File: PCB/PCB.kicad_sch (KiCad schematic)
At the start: 0 parts

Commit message: add symbols
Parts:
- added J1, J3, J5, J6: Conn_01x06_Socket, Connector_PinHeader_2.54mm:PinHeader_1x06_P2.54mm_Vertical, symbol Connector:Conn_01x06_Socket
- added J2, J4, J7, J8: Conn_01x04_Socket, Connector_PinHeader_2.54mm:PinHeader_1x04_P2.54mm_Vertical, symbol Connector:Conn_01x04_Socket
- added SW1, SW2, SW3: SW_Push, Connector_PinHeader_2.54mm:PinHeader_2x01_P2.54mm_Vertical, symbol Switch:SW_Push
- added U1, U2, U3, U4: HX711, symbol _HX711:HX711_Dev
- added U5: SD1306, Connector_PinHeader_2.54mm:PinHeader_1x04_P2.54mm_Vertical, symbol Display_Graphic:ER_OLEDM0.91_1x-I2C
- added U6: SD1309, Connector_PinHeader_2.54mm:PinHeader_1x04_P2.54mm_Vertical, symbol Display_Graphic:ER_OLEDM0.91_1x-I2C
- added U8: ESP32-DevKitC, PCM_Espressif:ESP32-DevKitC, symbol PCM_Espressif:ESP32-DevKitC
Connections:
- new net: J3.6 (Pin_6), U2.1 (E+)
- new net: J3.5 (Pin_5), U2.2 (E-)
- new net: J3.4 (Pin_4), U2.3 (A-)
- new net: J3.3 (Pin_3), U2.4 (A+)
- new net: J3.2 (Pin_2), U2.5 (B-)
- new net: J3.1 (Pin_1), U2.6 (B+)
- new net: J4.3 (Pin_3), U2.8 (DATA)
- new net: J4.2 (Pin_2), U2.9 (CLK)
- new net: J8.2 (Pin_2), U4.9 (CLK)
- new net: J8.3 (Pin_3), U4.8 (DATA)
- new net: J7.2 (Pin_2), U3.9 (CLK)
- new net: J7.3 (Pin_3), U3.8 (DATA)
- new net: J6.1 (Pin_1), U4.6 (B+)
- new net: J6.2 (Pin_2), U4.5 (B-)
- new net: J6.3 (Pin_3), U4.4 (A+)
- new net: J6.4 (Pin_4), U4.3 (A-)
- new net: J6.5 (Pin_5), U4.2 (E-)
- new net: J6.6 (Pin_6), U4.1 (E+)
- new net: J1.1 (Pin_1), U1.6 (B+)
- new net: J1.2 (Pin_2), U1.5 (B-)
- new net: J1.3 (Pin_3), U1.4 (A+)
- new net: J1.4 (Pin_4), U1.3 (A-)
- new net: J1.5 (Pin_5), U1.2 (E-)
- new net: J1.6 (Pin_6), U1.1 (E+)
- new net: J5.1 (Pin_1), U3.6 (B+)
- new net: J5.2 (Pin_2), U3.5 (B-)
- new net: J5.3 (Pin_3), U3.4 (A+)
- new net: J5.4 (Pin_4), U3.3 (A-)
- new net: J5.5 (Pin_5), U3.2 (E-)
- new net: J5.6 (Pin_6), U3.1 (E+)
- new net: J2.3 (Pin_3), U1.8 (DATA)
- new net: J2.2 (Pin_2), U1.9 (CLK)
- new net +3.3V: J2.1 (Pin_1), J4.1 (Pin_1), J7.1 (Pin_1), J8.1 (Pin_1), SW1.1, SW2.1, SW3.1, U1.10 (VCC), U2.10 (VCC), U3.10 (VCC), U4.10 (VCC), U5.2 (VCC), U6.2 (VCC), U8.1 (3V3)
- new net GND: J2.4 (Pin_4), J4.4 (Pin_4), J7.4 (Pin_4), J8.4 (Pin_4), U1.7 (GND), U2.7 (GND), U3.7 (GND), U4.7 (GND), U5.1 (GND), U6.1 (GND), U8.14 (GND), U8.32 (GND), U8.38 (GND)
- no-connect marks 0 -> 1

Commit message: Connect parts
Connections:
- net BTN1: now reaches SW1.2
- net BTN1: now also U8.27 (GPIO16)
- net DATA2: now reaches J4.3 (Pin_3), U2.8 (DATA)
- net DATA2: now also U8.7 (32K_XP/GPIO32/ADC1_CH4)
- net CLK2: now reaches J4.2 (Pin_2), U2.9 (CLK)
- net CLK2: now also U8.8 (32K_XN/GPIO33/ADC1_CH5)
- net CLK4: now reaches J8.2 (Pin_2), U4.9 (CLK)
- net CLK4: now also U8.12 (MTMS/GPIO14/ADC2_CH6)
- net DATA4: now reaches J8.3 (Pin_3), U4.8 (DATA)
- net DATA4: now also U8.11 (ADC2_CH7/GPIO27)
- net CLK3: now reaches J7.2 (Pin_2), U3.9 (CLK)
- net CLK3: now also U8.10 (DAC_2/ADC2_CH9/GPIO26)
- net DATA3: now reaches J7.3 (Pin_3), U3.8 (DATA)
- net DATA3: now also U8.9 (DAC_1/ADC2_CH8/GPIO25)
- net at U5.3 (SCL): now also U6.3 (SCL), U8.36 (GPIO22)
- net at U5.4 (SDA): now also U6.4 (SDA), U8.33 (GPIO21)
- net BTN3: now reaches SW3.2
- net BTN3: now also U8.29 (GPIO5)
- net BTN2: now reaches U8.28 (GPIO17)
- net BTN2: now also SW2.2
- net DATA1: now reaches U8.30 (GPIO18)
- net DATA1: now also J2.3 (Pin_3), U1.8 (DATA)
- net CLK1: now reaches U8.31 (GPIO19)
- net CLK1: now also J2.2 (Pin_2), U1.9 (CLK)
- no-connect marks 1 -> 21

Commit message: Finished layout
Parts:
- removed J1, J3, J5, J6: Conn_01x06_Socket, Connector_PinHeader_2.54mm:PinHeader_1x06_P2.54mm_Vertical, symbol Connector:Conn_01x06_Socket
- renumbered J2 to J1, J4 to J2, J7 to J3, J8 to J4, U8 to U5, U5 to U6, U6 to U7
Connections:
- no-connect marks 21 -> 45
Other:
- note added: "Adding capacitors will be helpful"

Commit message: update pcb
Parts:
- U5: footprint PCM_Espressif:ESP32-DevKitC -> _custom-footprint:ESP32-DevKitC
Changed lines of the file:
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@@
 			)
 		)
-		(property "Footprint" "PCM_Espressif:ESP32-DevKitC"
+		(property "Footprint" "_custom-footprint:ESP32-DevKitC"
 			(at 173.99 149.86 0)
 			(hide yes)

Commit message: Add capacitor
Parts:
- added C1: 10nf, Capacitor_THT:C_Radial_D5.0mm_H11.0mm_P2.00mm, symbol Device:C_Small_US
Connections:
- net +3.3V: now also C1.1
- net GND: now also C1.2
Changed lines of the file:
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@@
+	)
+	(symbol
+		(lib_id "power:VCC")
+		(at 109.22 171.45 0)
+		(unit 1)
+		(body_style 1)
+		(exclude_from_sim no)
+		(in_bom yes)
+		(on_board yes)
+		(in_pos_files yes)
+		(dnp no)
+		(fields_autoplaced yes)
+		(property "Reference" "#PWR022"
+			(at 109.22 175.26 0)
+			(hide yes)
+			(show_name no)
+			(do_not_autoplace no)
+			(effects
+				(font
+					(size 1.27 1.27)
+				)
+			)
+		)
+		(property "Value" "VCC"
+			(at 109.22 166.37 0)
+			(show_name no)
+			(do_not_autoplace no)
+			(effects
+				(font
+					(size 1.27 1.27)
+				)
+			)
+		)
+		(property "Footprint" ""
+			(at 109.22 171.45 0)
+			(hide yes)
+			(show_name no)
+			(do_not_autoplace no)
+			(effects
+				(font
+					(size 1.27 1.27)
+				)
+			)
+		)
+		(property "Datasheet" ""
+			(at 109.22 171.45 0)
+			(hide yes)
+			(show_name no)
+			(do_not_autoplace no)
+			(effects
+				(font
+					(size 1.27 1.27)
+				)
+			)
+		)
+		(property "Description" "Power symbol creates a global label with name \"VCC\""
+			(at 109.22 171.45 0)
+			(hide yes)
+			(show_name no)
+			(do_not_autoplace no)
+			(effects
+				(font
+					(size 1.27 1.27)
+				)
+			)
+		)
+		(pin "1"
+		)
+		(instances
+			(project "PCB"
+				(path "/dfd5a8fa-84d7-4b09-a8df-d6a914f2fe00"
+					(reference "#PWR022")
+					(unit 1)
+				)
+			)
+		)
 	)
 	(symbol
@@
 	)
 	(symbol
+		(lib_id "power:GND")
+		(at 109.22 176.53 0)
+		(unit 1)
+		(body_style 1)
+		(exclude_from_sim no)
+		(in_bom yes)
+		(on_board yes)
+		(in_pos_files yes)
+		(dnp no)
+		(fields_autoplaced yes)
+		(property "Reference" "#PWR021"
+			(at 109.22 182.88 0)
+			(hide yes)
+			(show_name no)
+			(do_not_autoplace no)
+			(effects
+				(font
+					(size 1.27 1.27)
+				)
+			)
+		)
+		(property "Value" "GND"
+			(at 109.22 181.61 0)
+			(hide yes)
+			(show_name no)
+			(do_not_autoplace no)
+			(effects
+				(font
+					(size 1.27 1.27)
+				)
+			)
+		)
+		(property "Footprint" ""
+			(at 109.22 176.53 0)
+			(hide yes)
+			(show_name no)
+			(do_not_autoplace no)
+			(effects
+				(font
+					(size 1.27 1.27)
+				)
+			)
+		)
+		(property "Datasheet" ""
+			(at 109.22 176.53 0)
+			(hide yes)
+			(show_name no)
+			(do_not_autoplace no)
+			(effects
+				(font
+					(size 1.27 1.27)
+				)
+			)
+		)
+		(property "Description" "Power symbol creates a global label with name \"GND\" , ground"
+			(at 109.22 176.53 0)
+			(hide yes)
+			(show_name no)
+			(do_not_autoplace no)
+			(effects
+				(font
+					(size 1.27 1.27)
+				)
+			)
+		)
+		(pin "1"
+		)
+		(instances
+			(project "PCB"
+				(path "/dfd5a8fa-84d7-4b09-a8df-d6a914f2fe00"
+					(reference "#PWR021")
+					(unit 1)
+				)
+			)
+		)
+	)
+	(symbol
 		(lib_id "_HX711:HX711_Dev")
 		(at 71.12 34.29 0)
@@
 					(unit 1)
 				)
+			)
+		)
+	)
+	(symbol
+		(lib_id "Device:C_Small_US")
+		(at 109.22 173.99 0)
+		(unit 1)
+		(body_style 1)
+		(exclude_from_sim no)
+		(in_bom yes)
+		(on_board yes)
+		(in_pos_files yes)
+		(dnp no)
+		(fields_autoplaced yes)
+		(property "Reference" "C1"
+			(at 111.76 172.8469 0)
+			(show_name no)
+			(do_not_autoplace no)
+			(effects
+				(font
+					(size 1.27 1.27)
+				)
+				(justify left)
+			)
+		)
+		(property "Value" "10nf"
+			(at 111.76 175.3869 0)
+			(show_name no)
+			(do_not_autoplace no)
+			(effects
+				(font
+					(size 1.27 1.27)
+				)
+				(justify left)
+			)
+		)
+		(property "Footprint" "Capacitor_THT:C_Radial_D5.0mm_H11.0mm_P2.00mm"
+			(at 109.22 173.99 0)
+			(hide yes)
+			(show_name no)
+			(do_not_autoplace no)
+			(effects
+				(font
+					(size 1.27 1.27)
+				)
+			)
+		)
+		(property "Datasheet" ""
+			(at 109.22 173.99 0)
+			(hide yes)
+			(show_name no)
+			(do_not_autoplace no)
+			(effects
+				(font
+					(size 1.27 1.27)
+				)
+			)
+		)
+		(property "Description" "capacitor, small US symbol"
+			(at 109.22 173.99 0)
+			(hide yes)
+			(show_name no)
+			(do_not_autoplace no)
+			(effects
+				(font
+					(size 1.27 1.27)
+				)
+			)
+		)
+		(pin "1"
+		)
+		(pin "2"
+		)
+		(instances
+			(project "PCB"
+				(path "/dfd5a8fa-84d7-4b09-a8df-d6a914f2fe00"
+					(reference "C1")
+					(unit 1)
+				)

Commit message: Change push button connection
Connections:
- net +3.3V: no longer SW1.1, SW2.1, SW3.1
- net GND: now also SW1.1, SW2.1, SW3.1
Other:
- note added: "Place capacitor near push buttons"
- note removed: "Adding capacitors will be helpful"
- moved on the sheet: C1

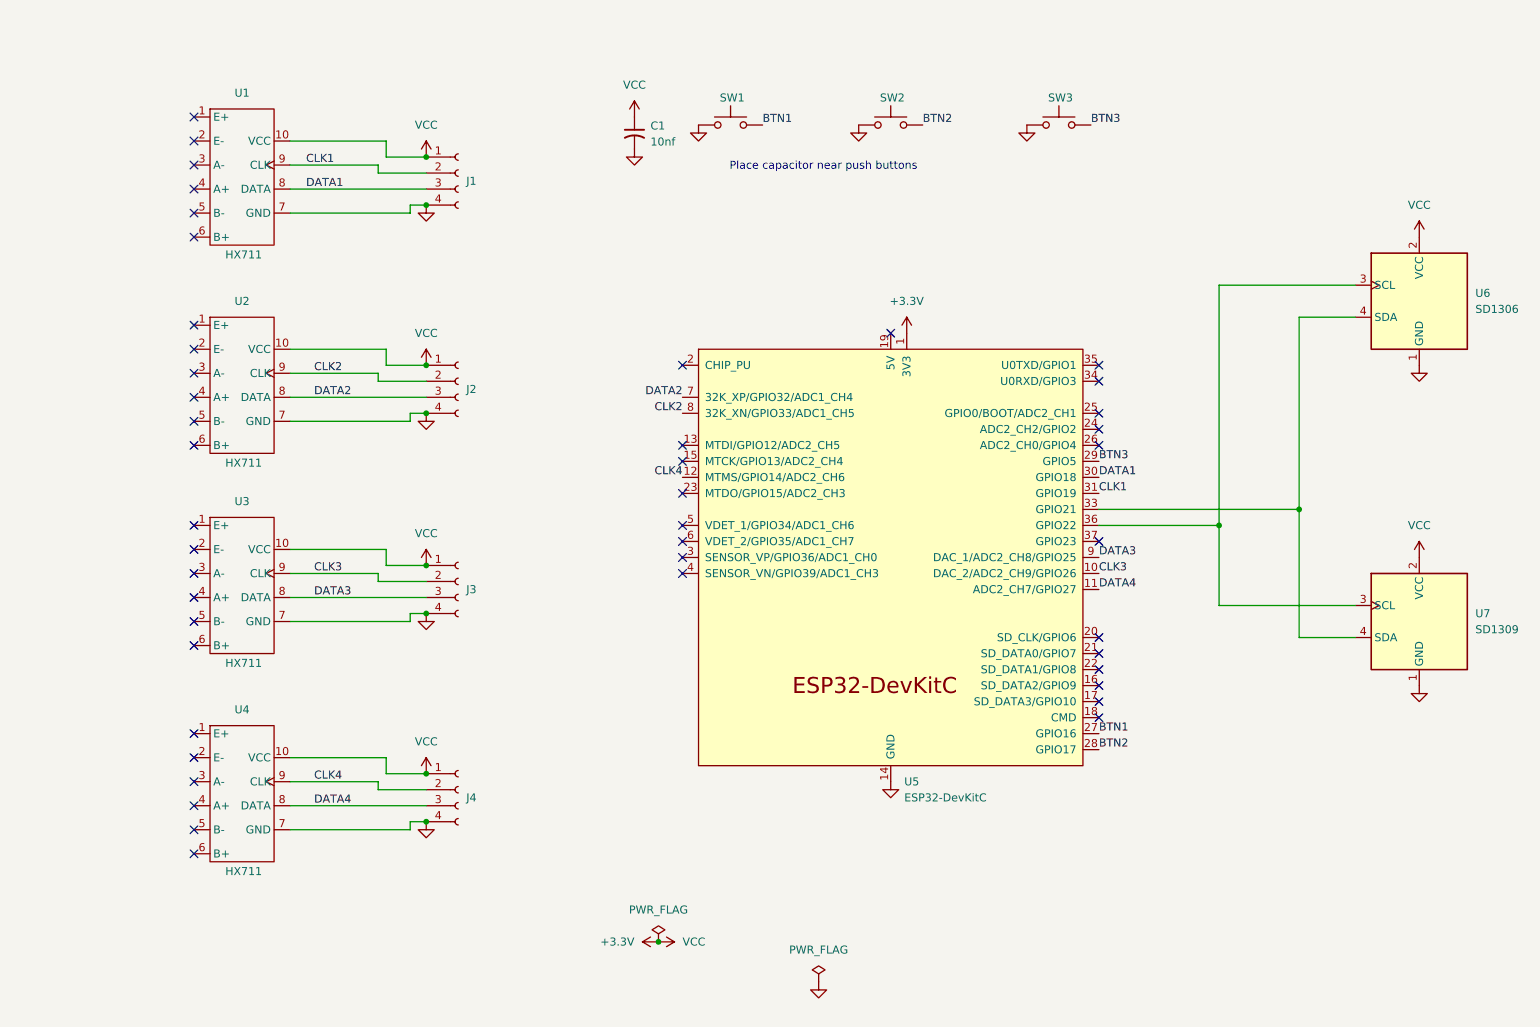
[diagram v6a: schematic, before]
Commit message: Add hardware deboucers at push buttons
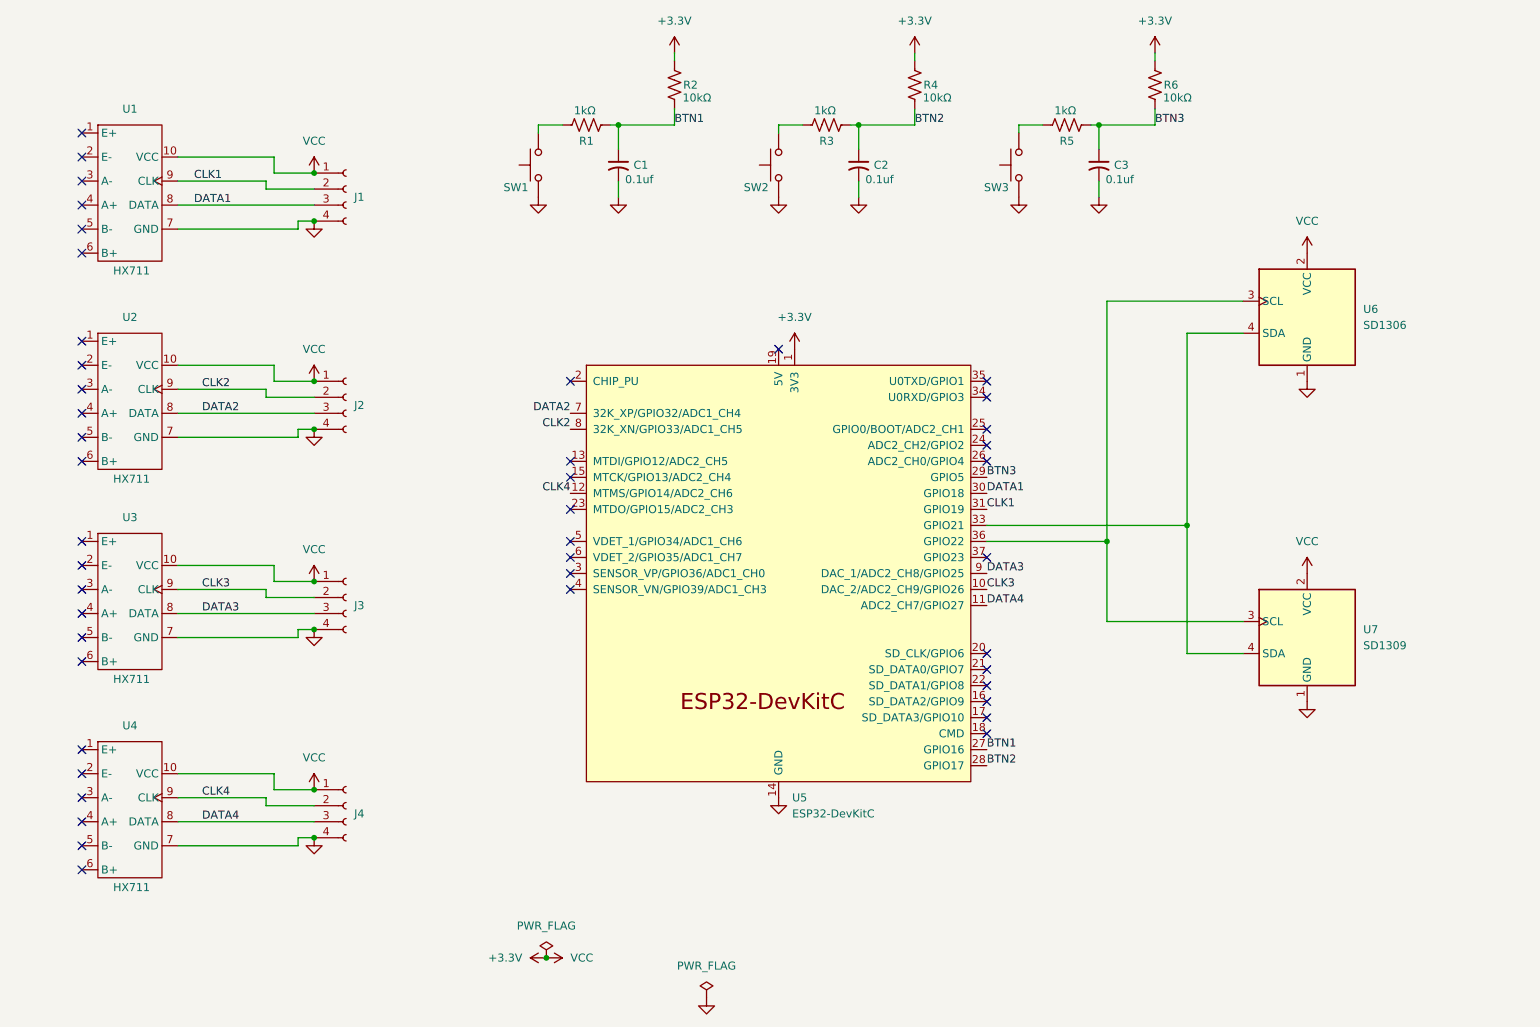
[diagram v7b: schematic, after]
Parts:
- added C2, C3: 0.1uf, Capacitor_THT:C_Radial_D5.0mm_H11.0mm_P2.00mm, symbol Device:C_Small_US
- added R1, R3, R5: 1kΩ, Resistor_THT:R_Axial_DIN0207_L6.3mm_D2.5mm_P10.16mm_Horizontal, symbol Device:R_US
- added R2, R4, R6: 10kΩ, Resistor_THT:R_Axial_DIN0207_L6.3mm_D2.5mm_P10.16mm_Horizontal, symbol Device:R_US
- C1: value 10nf -> 0.1uf
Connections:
- net +3.3V: now also R2.2, R4.2, R6.2; no longer C1.1
- net BTN1: now also C1.1, R1.2, R2.1; no longer SW1.2
- net BTN2: now also C2.1, R3.2, R4.1; no longer SW2.2
- net BTN3: now also C3.1, R5.2, R6.1; no longer SW3.2
- net GND: now also C2.2, C3.2
- new net: R1.1, SW1.2
- new net: R3.1, SW2.2
- new net: R5.1, SW3.2
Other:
- note removed: "Place capacitor near push buttons"
- moved on the sheet: C1, J1, J2, J3, J4, SW1, U1, U2, U3, U4, U5, U6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

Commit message: backup before routing hw debouncer
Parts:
- added JP1, JP2, JP3: Short this route to use software deboucer, Jumper:SolderJumper-2_P1.3mm_Open_Pad1.0x1.5mm, symbol Jumper:SolderJumper_2_Open
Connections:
- net BTN1: now also JP1.2 (B)
- net BTN2: now also JP2.2 (B)
- net BTN3: now also JP3.2 (B)
- net at R1.1, SW1.2: now also JP1.1 (A)
- net at R3.1, SW2.2: now also JP2.1 (A)
- net at R5.1, SW3.2: now also JP3.1 (A)
